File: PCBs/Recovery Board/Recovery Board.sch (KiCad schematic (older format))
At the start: 16 parts, among them J1 Conn_01x02, J2 Conn_01x02, J3 Conn_01x02, J4 Conn_01x02, J5 Conn_01x02, U1 R-78E3.3-0.5, X1 XBee-S2C

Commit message: added some new parts and i2c bus changes
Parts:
- renumbered 2k1 to 2k, 3k1 to 3k
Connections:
- net INSTRUMENT_ARDUINO_COMMS1 renamed SCL
- net SCL: now also A1.24 (AD5/D19); no longer A1.23 (AD4/D18)
- net INSTRUMENT_ARDUINO_COMMS2 renamed SDA
- net SDA: now also A1.23 (AD4/D18); no longer A1.24 (AD5/D19)
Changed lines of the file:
@@
 XBEE-DOUT
 Text GLabel 3250 6150 2    60   Input Italic 0
-INSTRUMENT_ARDUINO_COMMS1
+SDA
 Text GLabel 3250 6250 2    60   Input Italic 0
-INSTRUMENT_ARDUINO_COMMS2
+SCL
 Wire Wire Line
 	7300 4200 7750 4200
@@
 	4600 5650 3250 5650
 $Comp
-L R 2k1
+L R 2k
 U 1 1 5A8B21DB
 P 6600 5600
-F 0 "2k1" V 6680 5600 50  0000 C CNN
+F 0 "2k" V 6680 5600 50  0000 C CNN
 F 1 "R3" V 6600 5600 50  0000 C CNN
 F 2 "Resistors_SMD:R_0805_HandSoldering" V 6530 5600 50  0001 C CNN
@@
 $EndComp
 $Comp
-L R 3k1
+L R 3k
 U 1 1 5A8B22A6
 P 6600 6300
-F 0 "3k1" V 6680 6300 50  0000 C CNN
+F 0 "3k" V 6680 6300 50  0000 C CNN
 F 1 "R4" V 6600 6300 50  0000 C CNN
 F 2 "Resistors_SMD:R_0805_HandSoldering" V 6530 6300 50  0001 C CNN
@@
 $EndComp
 Text GLabel 2600 1200 2    60   Input Italic 0
-INSTRUMENT_ARDUINO_COMMS1
+SCL
 Text GLabel 2600 1100 2    60   Input Italic 0
-INSTRUMENT_ARDUINO_COMMS2
+SDA
 $Comp
 L R-78E3.3-0.5 U1

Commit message: stashing changes
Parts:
- added C?: 1uF, Capacitors_SMD:C_0805_HandSoldering, symbol C
- added C?: 8.2pF, Capacitors_SMD:C_0805_HandSoldering, symbol C
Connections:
- net GND: now also C?.2, C?.2
- net at C2.1, U1.3 (+Vout), X1.1 (Vcc): now also C?.1, C?.1
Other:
- moved on the sheet: C1, C2, U1
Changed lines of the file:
@@
 SCL
 Wire Wire Line
-	7300 4200 7750 4200
+	6850 4200 7750 4200
 $Comp
 L CPC1002N S1
@@
 Wire Wire Line
 	6600 6450 6600 6600
-Text GLabel 5600 4200 0    60   Input ~ 0
+Text GLabel 5150 4200 0    60   Input ~ 0
 7.4V
 Wire Wire Line
@@
 Connection ~ 6900 2400
 Wire Wire Line
-	7500 4750 7500 4750
-Wire Wire Line
-	7500 4750 7500 4600
-Wire Wire Line
-	7500 4300 7500 4200
-Connection ~ 7500 4200
+	7050 4750 7050 4750
+Wire Wire Line
+	7050 4750 7050 4600
+Wire Wire Line
+	7050 4300 7050 4200
+Connection ~ 7050 4200
 Text Notes 7200 5850 2    60   ~ 0
 3.3V data
-Text Notes 7750 4150 2    60   ~ 0
+Text Notes 7300 4150 2    60   ~ 0
 3.3V power
-Connection ~ 6050 4200
+Connection ~ 5600 4200
 $Comp
 L Conn_01x02 J5
@@
 L GND #PWR02
 U 1 1 5A9AC98C
-P 6050 4750
-F 0 "#PWR02" H 6050 4500 50  0001 C CNN
-F 1 "GND" H 6050 4600 50  0000 C CNN
-F 2 "" H 6050 4750 50  0001 C CNN
-F 3 "" H 6050 4750 50  0001 C CNN
-	1    6050 4750
+P 5600 4750
+F 0 "#PWR02" H 5600 4500 50  0001 C CNN
+F 1 "GND" H 5600 4600 50  0000 C CNN
+F 2 "" H 5600 4750 50  0001 C CNN
+F 3 "" H 5600 4750 50  0001 C CNN
+	1    5600 4750
 	1    0    0    -1
 $EndComp
@@
 L GND #PWR03
 U 1 1 5A9ACBA8
-P 6750 4650
-F 0 "#PWR03" H 6750 4400 50  0001 C CNN
-F 1 "GND" H 6750 4500 50  0000 C CNN
-F 2 "" H 6750 4650 50  0001 C CNN
-F 3 "" H 6750 4650 50  0001 C CNN
-	1    6750 4650
+P 6300 4650
+F 0 "#PWR03" H 6300 4400 50  0001 C CNN
+F 1 "GND" H 6300 4500 50  0000 C CNN
+F 2 "" H 6300 4650 50  0001 C CNN
+F 3 "" H 6300 4650 50  0001 C CNN
+	1    6300 4650
 	1    0    0    -1
 $EndComp
@@
 L GND #PWR05
 U 1 1 5A9AD339
-P 7500 4750
-F 0 "#PWR05" H 7500 4500 50  0001 C CNN
-F 1 "GND" H 7500 4600 50  0000 C CNN
-F 2 "" H 7500 4750 50  0001 C CNN
-F 3 "" H 7500 4750 50  0001 C CNN
-	1    7500 4750
+P 7050 4750
+F 0 "#PWR05" H 7050 4500 50  0001 C CNN
+F 1 "GND" H 7050 4600 50  0000 C CNN
+F 2 "" H 7050 4750 50  0001 C CNN
+F 3 "" H 7050 4750 50  0001 C CNN
+	1    7050 4750
 	1    0    0    -1
 $EndComp
@@
 L C C1
 U 1 1 5A9AEA7D
-P 6050 4450
-F 0 "C1" H 6075 4550 50  0000 L CNN
-F 1 "10uF" H 6075 4350 50  0000 L CNN
-F 2 "Capacitors_SMD:C_0805_HandSoldering" H 6088 4300 50  0001 C CNN
-F 3 "" H 6050 4450 50  0001 C CNN
-	1    6050 4450
+P 5600 4450
+F 0 "C1" H 5625 4550 50  0000 L CNN
+F 1 "10uF" H 5625 4350 50  0000 L CNN
+F 2 "Capacitors_SMD:C_0805_HandSoldering" H 5638 4300 50  0001 C CNN
+F 3 "" H 5600 4450 50  0001 C CNN
+	1    5600 4450
 	1    0    0    -1
 $EndComp
@@
 L C C2
 U 1 1 5A9AEB07
-P 7500 4450
-F 0 "C2" H 7525 4550 50  0000 L CNN
-F 1 "10uF" H 7525 4350 50  0000 L CNN
-F 2 "Capacitors_SMD:C_0805_HandSoldering" H 7538 4300 50  0001 C CNN
-F 3 "" H 7500 4450 50  0001 C CNN
-	1    7500 4450
+P 7050 4450
+F 0 "C2" H 7075 4550 50  0000 L CNN
+F 1 "10uF" H 7075 4350 50  0000 L CNN
+F 2 "Capacitors_SMD:C_0805_HandSoldering" H 7088 4300 50  0001 C CNN
+F 3 "" H 7050 4450 50  0001 C CNN
+	1    7050 4450
 	1    0    0    -1
 $EndComp
@@
 L R-78E3.3-0.5 U1
 U 1 1 5A9B412D
-P 6750 4350
-F 0 "U1" H 6750 4800 60  0000 C CNN
-F 1 "R-78E3.3-0.5" H 6750 3750 60  0000 C CNN
-F 2 "sip:SIP3" H 6750 4350 60  0001 C CNN
-F 3 "" H 6750 4350 60  0001 C CNN
-	1    6750 4350
-	1    0    0    -1
-$EndComp
-Wire Wire Line
-	5600 4200 6200 4200
-Wire Wire Line
-	6050 4300 6050 4200
-Wire Wire Line
-	6050 4600 6050 4750
+P 6300 4350
+F 0 "U1" H 6300 4800 60  0000 C CNN
+F 1 "R-78E3.3-0.5" H 6300 3750 60  0000 C CNN
+F 2 "sip:SIP3" H 6300 4350 60  0001 C CNN
+F 3 "" H 6300 4350 60  0001 C CNN
+	1    6300 4350
+	1    0    0    -1
+$EndComp
+Wire Wire Line
+	5150 4200 5750 4200
+Wire Wire Line
+	5600 4300 5600 4200
+Wire Wire Line
+	5600 4600 5600 4750
+Wire Wire Line
+	7300 4750 7300 4750
+Wire Wire Line
+	7300 4750 7300 4600
+Wire Wire Line
+	7300 4200 7300 4300
+$Comp
+L GND #PWR?
+U 1 1 5ABA400A
+P 7300 4750
+F 0 "#PWR?" H 7300 4500 50  0001 C CNN
+F 1 "GND" H 7300 4600 50  0000 C CNN
+F 2 "" H 7300 4750 50  0001 C CNN
+F 3 "" H 7300 4750 50  0001 C CNN
+	1    7300 4750
+	1    0    0    -1
+$EndComp
+$Comp
+L C C?
+U 1 1 5ABA4010
+P 7300 4450
+F 0 "C?" H 7325 4550 50  0000 L CNN
+F 1 "1uF" H 7325 4350 50  0000 L CNN
+F 2 "Capacitors_SMD:C_0805_HandSoldering" H 7338 4300 50  0001 C CNN
+F 3 "" H 7300 4450 50  0001 C CNN
+	1    7300 4450
+	1    0    0    -1
+$EndComp
+Wire Wire Line
+	7550 4750 7550 4750
+Wire Wire Line
+	7550 4750 7550 4600
+Wire Wire Line
+	7550 4200 7550 4300
+$Comp
+L GND #PWR?
+U 1 1 5ABA4092
+P 7550 4750
+F 0 "#PWR?" H 7550 4500 50  0001 C CNN
+F 1 "GND" H 7550 4600 50  0000 C CNN
+F 2 "" H 7550 4750 50  0001 C CNN
+F 3 "" H 7550 4750 50  0001 C CNN
+	1    7550 4750
+	1    0    0    -1
+$EndComp
+$Comp
+L C C?
+U 1 1 5ABA4098
+P 7550 4450
+F 0 "C?" H 7575 4550 50  0000 L CNN
+F 1 "8.2pF" H 7575 4350 50  0000 L CNN
+F 2 "Capacitors_SMD:C_0805_HandSoldering" H 7588 4300 50  0001 C CNN
+F 3 "" H 7550 4450 50  0001 C CNN
+	1    7550 4450
+	1    0    0    -1
+$EndComp
+Connection ~ 7300 4200
+Connection ~ 7550 4200
 $EndSCHEMATC

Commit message: added various review changes
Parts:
- added J6: Conn_01x02, Connectors_Molex:Molex_KK-6410-02_02x2.54mm_Straight, symbol Conn_01x02
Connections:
- net GND: now also J6.1 (Pin_1)
- net XBEE-DOUT: no longer A1.1 (D1/RX)
- net Sheet5ABE85A8/A: now reaches A1.5 (D2)
- net 3.3V: now reaches C2.1, C?.1, C?.1, U1.3 (+Vout), X1.1 (Vcc)
- new net Sheet5ABE85A8/A: A1.1 (D1/RX)
- new net Stratologger_TX: J6.2 (Pin_2)
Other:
- moved on the sheet: 2k, 3k, C1, C2, C?, J1, J2, J3, J4, J5, R1, R2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

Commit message: swapped TX and RX pins
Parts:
- A1: symbol Arduino_Nano -> Arduino_Nano-RESCUE-Recovery_Board
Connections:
- net Sheet5ABE85A8/A is gone; now on net Sheet5ABE85A8/A: A1.5 (D2)
- net Sheet5ABE85A8/A: no longer A1.1 (D1/RX)
- net XBEE-DIN: now also A1.1 (D0/TX); no longer A1.2 (D0/TX)
- new net Sheet5ABE85A8/A: A1.2 (D1/RX)
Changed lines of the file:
@@
 EESchema Schematic File Version 2
+LIBS:Recovery Board-rescue
 LIBS:power
 LIBS:device
@@
 $EndDescr
 $Comp
-L Arduino_Nano A1
+L Arduino_Nano-RESCUE-Recovery_Board A1
 U 1 1 5A446A9A
 P 2550 5400
 F 0 "A1" H 2550 5400 60  0000 C CNN
 F 1 "Arduino_Nano" H 2550 5550 60  0000 C CNN
-F 2 "Modules:Arduino_Nano" H 2550 5400 60  0001 C CNN
+F 2 "Modules:Arduino_Nano" H 2550 5400 60  0000 C CNN
 F 3 "" H 2550 5400 60  0000 C CNN
 	1    2550 5400

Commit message: review changes + instr board PCB
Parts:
- added R1, R2, R3, R4: 0, Resistors_SMD:R_0805_HandSoldering, symbol R
- R5: renamed from R1; value 1.9k -> 1.2k
- R6: renamed from R2; value 1.9k -> 1.2k
- R7: renamed from 2k; value R3 -> 2k
- R8: renamed from 3k; value R4 -> 3k
- gave numbers to parts that had none: 2
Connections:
- net Sheet5ABE85A8/A: now also R2.2, R3.2; no longer A1.2 (D1/RX)
- net XBEE-DIN: now also R1.2, R4.2; no longer A1.1 (D0/TX)
- net Sheet5ABE85A8/A: now reaches A1.11 (D8)
- net Stratologger_Relay: now reaches A1.15 (D12)
- net Stratologger_Relay: now also R6.2
- net Instr_Arduino_Relay: now reaches A1.16 (D13), R5.2
- net Instr_Arduino_Relay: no longer R6.2
- net at A1.6 (D3): now also R4.1
- net Sheet5ABE85A8/A: no longer names the net of A1.5 (D2)
- net Sheet5ABE85A8/A: now also R3.1
- new net: A1.1 (D0/TX), R1.1
- new net: A1.2 (D1/RX), R2.1

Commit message: Updated Recovery Netlist, started board updated layout
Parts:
- U1: footprint sip:SIP3 -> SparkFun-RF:SIP3
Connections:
- net Sheet5ABE85A8/A is gone; now on net Sheet5ABE85A8/A: R2.2, R3.2
- net Sheet5ABE85A8/A: no longer A1.11 (D8)
- new net Sheet5ABE85A8_2/A: A1.11 (D8)
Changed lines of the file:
@@
 LIBS:fgpmmopa6h
 LIBS:sot-223
-LIBS:Placeholders
 LIBS:Recovery Board Parts
 LIBS:ap2204k-5
@@
 $EndComp
 $Comp
-L GND #PWR11
+L GND #PWR01
 U 1 1 5A9AC8F8
 P 7550 6500
-F 0 "#PWR11" H 7550 6250 50  0001 C CNN
+F 0 "#PWR01" H 7550 6250 50  0001 C CNN
 F 1 "GND" H 7550 6350 50  0000 C CNN
 F 2 "" H 7550 6500 50  0001 C CNN
@@
 $EndComp
 $Comp
-L GND #PWR9
+L GND #PWR02
 U 1 1 5A9AC98C
 P 6550 4650
-F 0 "#PWR9" H 6550 4400 50  0001 C CNN
+F 0 "#PWR02" H 6550 4400 50  0001 C CNN
 F 1 "GND" H 6550 4500 50  0000 C CNN
 F 2 "" H 6550 4650 50  0001 C CNN
@@
 $EndComp
 $Comp
-L GND #PWR10
+L GND #PWR03
 U 1 1 5A9ACBA8
 P 7250 4550
-F 0 "#PWR10" H 7250 4300 50  0001 C CNN
+F 0 "#PWR03" H 7250 4300 50  0001 C CNN
 F 1 "GND" H 7250 4400 50  0000 C CNN
 F 2 "" H 7250 4550 50  0001 C CNN
@@
 $EndComp
 $Comp
-L GND #PWR15
+L GND #PWR04
 U 1 1 5A9AD16E
 P 8600 6000
-F 0 "#PWR15" H 8600 5750 50  0001 C CNN
+F 0 "#PWR04" H 8600 5750 50  0001 C CNN
 F 1 "GND" H 8600 5850 50  0000 C CNN
 F 2 "" H 8600 6000 50  0001 C CNN
@@
 $EndComp
 $Comp
-L GND #PWR12
+L GND #PWR05
 U 1 1 5A9AD339
 P 8000 4650
-F 0 "#PWR12" H 8000 4400 50  0001 C CNN
+F 0 "#PWR05" H 8000 4400 50  0001 C CNN
 F 1 "GND" H 8000 4500 50  0000 C CNN
 F 2 "" H 8000 4650 50  0001 C CNN
@@
 $EndComp
 $Comp
-L GND #PWR7
+L GND #PWR06
 U 1 1 5A9AD9D1
 P 6000 2500
-F 0 "#PWR7" H 6000 2250 50  0001 C CNN
+F 0 "#PWR06" H 6000 2250 50  0001 C CNN
 F 1 "GND" H 6000 2350 50  0000 C CNN
 F 2 "" H 6000 2500 50  0001 C CNN
@@
 $EndComp
 $Comp
-L GND #PWR8
+L GND #PWR07
 U 1 1 5A9ADA92
 P 6050 1450
-F 0 "#PWR8" H 6050 1200 50  0001 C CNN
+F 0 "#PWR07" H 6050 1200 50  0001 C CNN
 F 1 "GND" H 6050 1300 50  0000 C CNN
 F 2 "" H 6050 1450 50  0001 C CNN
@@
 $EndComp
 $Comp
-L GND #PWR2
+L GND #PWR08
 U 1 1 5A9ADD02
 P 1850 6450
-F 0 "#PWR2" H 1850 6200 50  0001 C CNN
+F 0 "#PWR08" H 1850 6200 50  0001 C CNN
 F 1 "GND" H 1850 6300 50  0000 C CNN
 F 2 "" H 1850 6450 50  0001 C CNN
@@
 $EndComp
 $Comp
-L GND #PWR1
+L GND #PWR09
 U 1 1 5A9ADED2
 P 1700 6450
-F 0 "#PWR1" H 1700 6200 50  0001 C CNN
+F 0 "#PWR09" H 1700 6200 50  0001 C CNN
 F 1 "GND" H 1700 6300 50  0000 C CNN
 F 2 "" H 1700 6450 50  0001 C CNN
@@
 $EndComp
 $Comp
-L GND #PWR3
+L GND #PWR010
 U 1 1 5A9AE056
 P 2950 3400
-F 0 "#PWR3" H 2950 3150 50  0001 C CNN
+F 0 "#PWR010" H 2950 3150 50  0001 C CNN
 F 1 "GND" H 2950 3250 50  0000 C CNN
 F 2 "" H 2950 3400 50  0001 C CNN
@@
 GoPro_Power
 $Comp
-L GND #PWR6
+L GND #PWR011
 U 1 1 5A9AF05A
 P 3850 2850
-F 0 "#PWR6" H 3850 2600 50  0001 C CNN
+F 0 "#PWR011" H 3850 2600 50  0001 C CNN
 F 1 "GND" H 3850 2700 50  0000 C CNN
 F 2 "" H 3850 2850 50  0001 C CNN
@@
 $EndComp
 $Comp
-L GND #PWR4
+L GND #PWR012
 U 1 1 5A9AF30B
 P 3350 1500
-F 0 "#PWR4" H 3350 1250 50  0001 C CNN
+F 0 "#PWR012" H 3350 1250 50  0001 C CNN
 F 1 "GND" H 3350 1350 50  0000 C CNN
 F 2 "" H 3350 1500 50  0001 C CNN
@@
 F 0 "U1" H 7250 4700 60  0000 C CNN
 F 1 "R-78E3.3-0.5" H 7250 3650 60  0000 C CNN
-F 2 "sip:SIP3" H 7250 4250 60  0001 C CNN
+F 2 "SparkFun-RF:SIP3" H 7250 4250 60  0001 C CNN
 F 3 "" H 7250 4250 60  0001 C CNN
 	1    7250 4250
@@
 $EndComp
 $Comp
-L GND #PWR13
+L GND #PWR013
 U 1 1 5ABA400A
 P 8250 4650
-F 0 "#PWR13" H 8250 4400 50  0001 C CNN
+F 0 "#PWR013" H 8250 4400 50  0001 C CNN
 F 1 "GND" H 8250 4500 50  0000 C CNN
 F 2 "" H 8250 4650 50  0001 C CNN
@@
 $EndComp
 $Comp
-L GND #PWR14
+L GND #PWR014
 U 1 1 5ABA4092
 P 8500 4650
-F 0 "#PWR14" H 8500 4400 50  0001 C CNN
+F 0 "#PWR014" H 8500 4400 50  0001 C CNN
 F 1 "GND" H 8500 4500 50  0000 C CNN
 F 2 "" H 8500 4650 50  0001 C CNN
@@
 $EndComp
 $Comp
-L GND #PWR5
+L GND #PWR015
 U 1 1 5ABE78A1
 P 3450 3900
-F 0 "#PWR5" H 3450 3650 50  0001 C CNN
+F 0 "#PWR015" H 3450 3650 50  0001 C CNN
 F 1 "GND" H 3450 3750 50  0000 C CNN
 F 2 "" H 3450 3900 50  0001 C CNN
@@
 S 4500 5650 700  450
 U 5ABEAE41
-F0 "Sheet5ABE85A8" 60
+F0 "Sheet5ABE85A8_2" 60
 F1 "file5ABE85A8.sch" 60
 F2 "A" I L 4500 6000 60

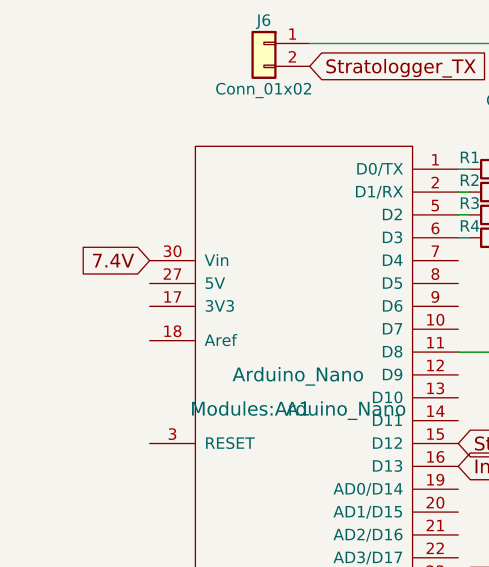
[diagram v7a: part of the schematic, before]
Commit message: Finished updating recovery board layout
board layout, schematic and netlist up to date
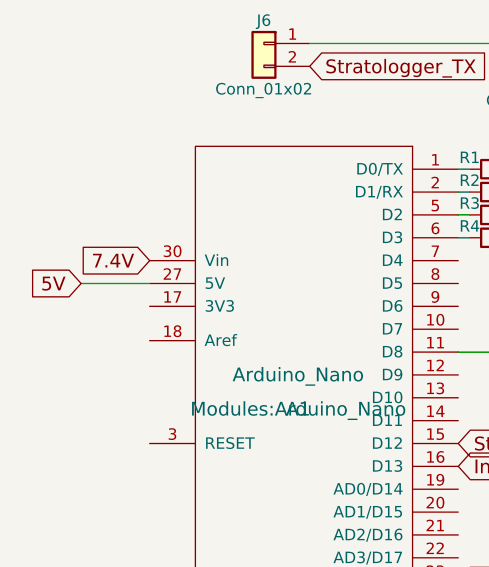
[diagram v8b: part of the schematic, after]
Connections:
- net 5V: now also A1.27 (5V)
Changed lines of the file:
@@
 Wire Wire Line
 	3250 4550 3300 4550
+Text GLabel 1600 4850 0    60   Input ~ 0
+5V
+Wire Wire Line
+	1900 4850 1600 4850
 $EndSCHEMATC
